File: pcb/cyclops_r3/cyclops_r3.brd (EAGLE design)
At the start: 69.8 x 53.3 mm, 78 parts, among them Q1 SUM11006, Q2 IRF510, U1 MCP4921, U2 TLV37, U3 317-N, U4 337-N, U5 ADR03, U6 OP1177, U7 LM324N, U8 ZXTD45

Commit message: While breadboarding the overcurrent protection circuit, I found a problem with the PFET power switch. Documented in notes, but not fixed yet.
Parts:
- C5: value 10pF -> 10nF
- R11: value 3.0k -> 3k
- R12: value 2.4k -> 3k
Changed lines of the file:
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@@
 <attribute name="NAME" x="14.813" y="20.8089" size="0.889" layer="26" font="vector" ratio="18" rot="MR180"/>
 </element>
-<element name="R12" library="cyclops" package="0603" value="2.4k" x="57.531" y="22.479" smashed="yes" rot="MR0">
+<element name="R12" library="cyclops" package="0603" value="3k" x="57.531" y="22.479" smashed="yes" rot="MR0">
 <attribute name="MN" value="Panasonic" x="56.007" y="39.243" size="1.6764" layer="28" ratio="18" rot="MR0" display="off"/>
 <attribute name="DK" value="PxxxxHTR-ND" x="56.007" y="39.243" size="1.6764" layer="28" ratio="18" rot="MR0" display="off"/>
@@
 <attribute name="VALUE" x="31.115" y="4.445" size="0.889" layer="28" font="vector" ratio="18" rot="MR0" align="center-left"/>
 </element>
-<element name="R11" library="cyclops" package="0603" value="3.0k" x="57.531" y="20.701" smashed="yes" rot="MR0">
+<element name="R11" library="cyclops" package="0603" value="3k" x="57.531" y="20.701" smashed="yes" rot="MR0">
 <attribute name="MN" value="Panasonic" x="56.134" y="27.305" size="1.6764" layer="28" ratio="18" rot="MR0" display="off"/>
 <attribute name="DK" value="PxxxxHTR-ND" x="56.134" y="27.305" size="1.6764" layer="28" ratio="18" rot="MR0" display="off"/>
@@
 <attribute name="VALUE" x="61.976" y="18.415" size="1.27" layer="27"/>
 </element>
-<element name="C5" library="cyclops" package="0603" value="10pF" x="39.116" y="6.604" smashed="yes" rot="MR180">
+<element name="C5" library="cyclops" package="0603" value="10nF" x="39.116" y="6.604" smashed="yes" rot="MR180">
 <attribute name="NAME" x="46.609" y="6.604" size="0.889" layer="26" font="vector" ratio="18" rot="MR180" align="center-right"/>
 <attribute name="VALUE" x="41.275" y="6.604" size="0.889" layer="28" font="vector" ratio="18" rot="MR180" align="center-left"/>
@@
 <wire x1="13.462" y1="27.94" x2="13.462" y2="26.416" width="0.4064" layer="16"/>
 <contactref element="VBIAS" pad="TP"/>
-<wire x1="17.018" y1="37.338" x2="17.018" y2="37.846" width="0" layer="19" extent="1-16"/>
 <wire x1="17.018" y1="37.846" x2="17.018" y2="39.116" width="0.4064" layer="16"/>
 <wire x1="18.362" y1="41.148" x2="22.292" y2="41.148" width="0.4064" layer="1"/>

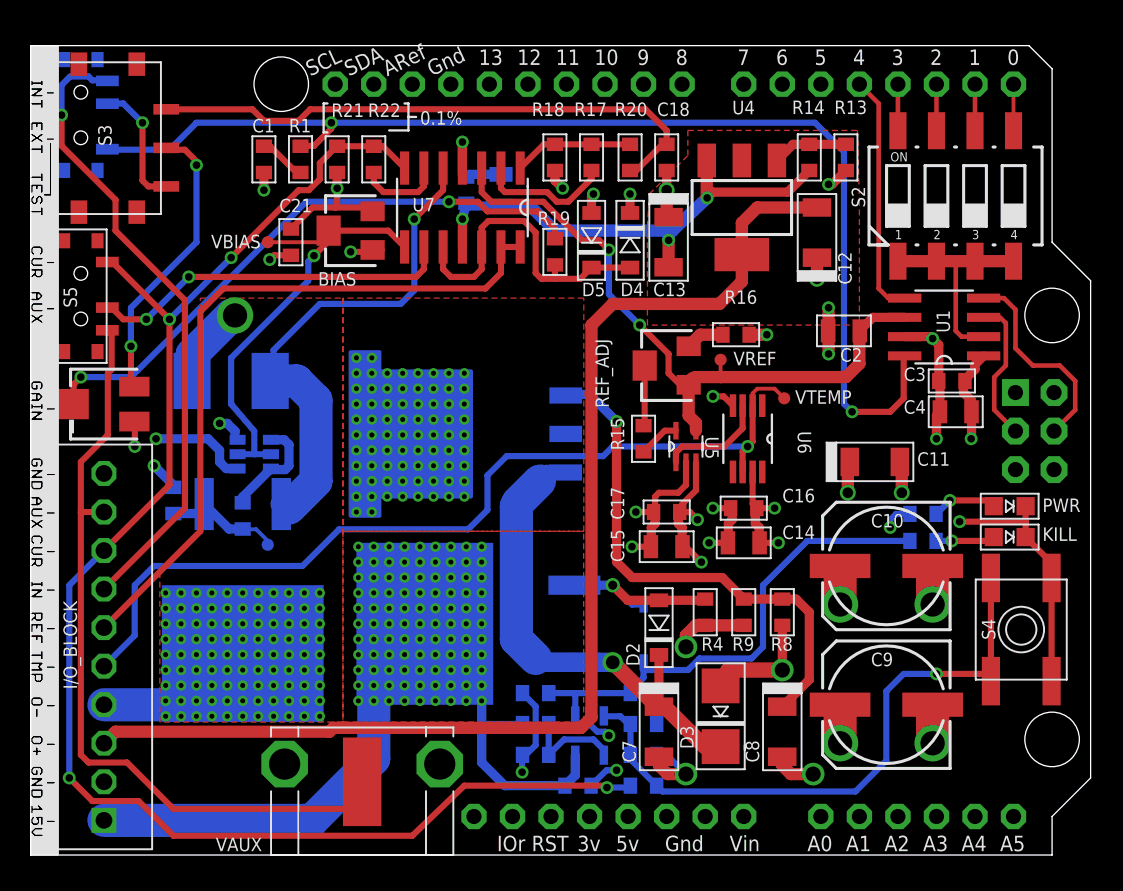
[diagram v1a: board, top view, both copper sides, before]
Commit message: Fixing the overcurrent protection circuit.
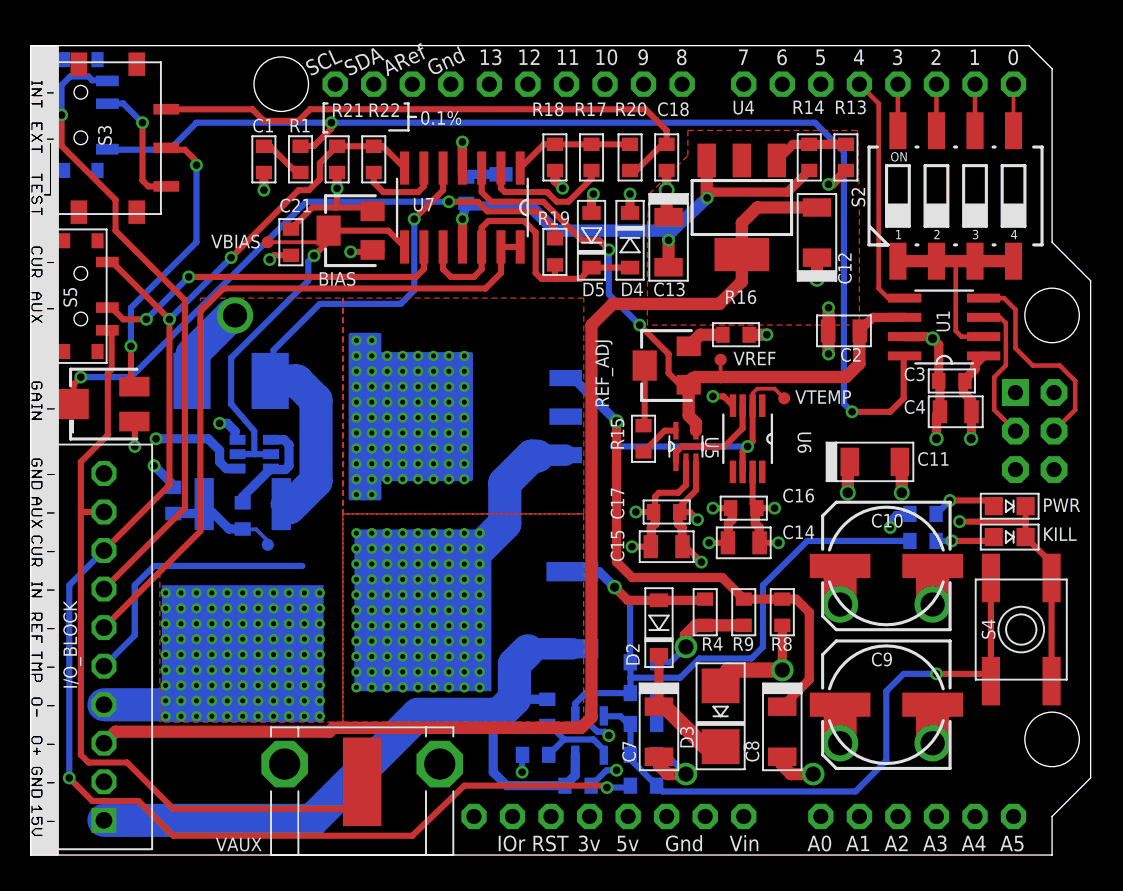
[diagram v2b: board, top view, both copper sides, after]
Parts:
- removed D1: (no value), cyclops:SOD-323F
- moved R10 7.40 mm to (39.1, 12.7), turned to 0 degrees
- moved U3 1.14 mm to (26.8, 28.9)
- moved R3 1.08 mm to (32.8, 9.40), turned to 270 degrees
- moved Q1 0.90 mm to (29.1, 16.1)
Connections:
- removed net +15V_RECT: C7.+, D2.C, D3.C, Q1.S, U3.3
- removed net N$18: D1.C, D2.A, Q1.G, R4.2
- new net +15V_ON: C7.+, D2.C, D3.C, Q1.D, U3.3
- net +15V: now also Q1.S; no longer Q1.D
- net KILL: now also D2.A, Q1.G, R4.2; no longer D1.A
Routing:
- net +15V_RECT: track 33.0 -> 0.00 mm, vias 1 -> 0
- net VTEMP: track 59.6 -> 34.6 mm
- net +15V_ON: track 0.00 -> 24.9 mm, vias 0 -> 99
- net KILL: track 32.7 -> 46.5 mm, vias 0 -> 1
- net N$18: track 11.6 -> 0.00 mm, vias 1 -> 0
- net +15V: track 47.2 -> 50.3 mm, vias 99 -> 0
- net GND: track 106.8 -> 104.3 mm
- net N$5: track 6.72 -> 6.19 mm
- added copper zone on layer 1, net +15V_ON
- removed copper zone on layer 1, net +15V

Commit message: Almost finished with the layout. I need to fix the top silskcreen which provides pin information.
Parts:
- removed D5: DS11015, cyclops:SOD123
- added C22: .1uF, cyclops:0603
- added D1: MMSZ, cyclops:SOD123
- C21: value .1uF -> ??
- D2: value MMSZ -> S1B; device cyclops:SOD123 -> cyclops:SMA-DO214AC
- D3: value S1B -> DS11015; device cyclops:SMA-DO214AC -> cyclops:SOD123
- KILL, PWR: value (none) -> LED
- R3: value 56k -> 10k
- R4: value 10k -> 56k
- U2: value TLV37 -> 317-N; device ti-extended:SOT95P280X145-5N -> cyclops:TO-263
- U3: value 317-N -> TLV37; device cyclops:TO-263 -> ti-extended:SOT95P280X145-5N
- U7: value LM324N -> TLV2374
- VAUX: value (none) -> 361V509E
- moved D3 31.9 mm to (38.2, 40.5), turned to 90 degrees
- moved U2 22.8 mm to (26.8, 28.9)
- moved U3 22.8 mm to (35.6, 7.87)
- moved C7 18.8 mm to (39.0, 26.9), turned to 90 degrees
- moved R3 12.3 mm to (43.2, 16.0), flipped to the top, turned to 90 degrees
- moved R4 12.3 mm to (32.8, 9.40), flipped to the bottom, turned to 270 degrees
- moved C21 8.09 mm to (21.8, 45.8), turned to 270 degrees
- moved D2 7.12 mm to (44.2, 9.14)
- moved R15 6.14 mm to (37.2, 33.3)
- moved D4 2.54 mm to (35.7, 40.5), turned to 270 degrees
- moved R1 1.91 mm to (14.6, 45.8)
- moved C1 1.90 mm to (12.2, 45.8)
- moved R21 1.90 mm to (17.0, 45.8)
- moved R22 1.90 mm to (19.4, 45.8)
- moved C11 0.25 mm to (54.1, 25.9)
- renumbered U$1 to ARDUNIO
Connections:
- net +12V: now also C22.1, D2.A, D3.C, U2.2, U2.4; no longer C21.1, D3.A, D4.C, U3.2, U3.4
- net +15V: now also R4.1, U3.5; no longer R3.1, U2.5
- net +15V_ON: now also D1.C, U2.3; no longer D3.C, U3.3
- net COMP+: now also U3.3; no longer U2.3
- net GND: now also C22.2, D4.A, R3.1, U3.2; no longer C21.2, D5.A, R4.1, U2.2
- net KILL: now also D1.A, R3.2, U3.1; no longer D2.A, R4.2, U2.1
- net N$15: now also C21.2
- net N$5: now also R4.2, U3.4; no longer R3.2, U2.4
- net N$72: now also U2.1; no longer U3.1
- net VI: now also C21.1
- net _VREF: now also D3.A, D4.C; no longer D4.A, D5.C
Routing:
- net VTEMP: track 34.6 -> 60.0 mm
- net +15V_ON: track 24.9 -> 49.1 mm, vias 99 -> 101
- net DACA: track 77.0 -> 69.6 mm
- net N$20: track 2.71 -> 7.42 mm, vias 0 -> 2
- net N$15: track 5.59 -> 8.84 mm
- net VI: track 100.2 -> 101.6 mm
- net GND: track 104.3 -> 102.9 mm, vias 31 -> 32
- net N$22: track 4.25 -> 3.64 mm

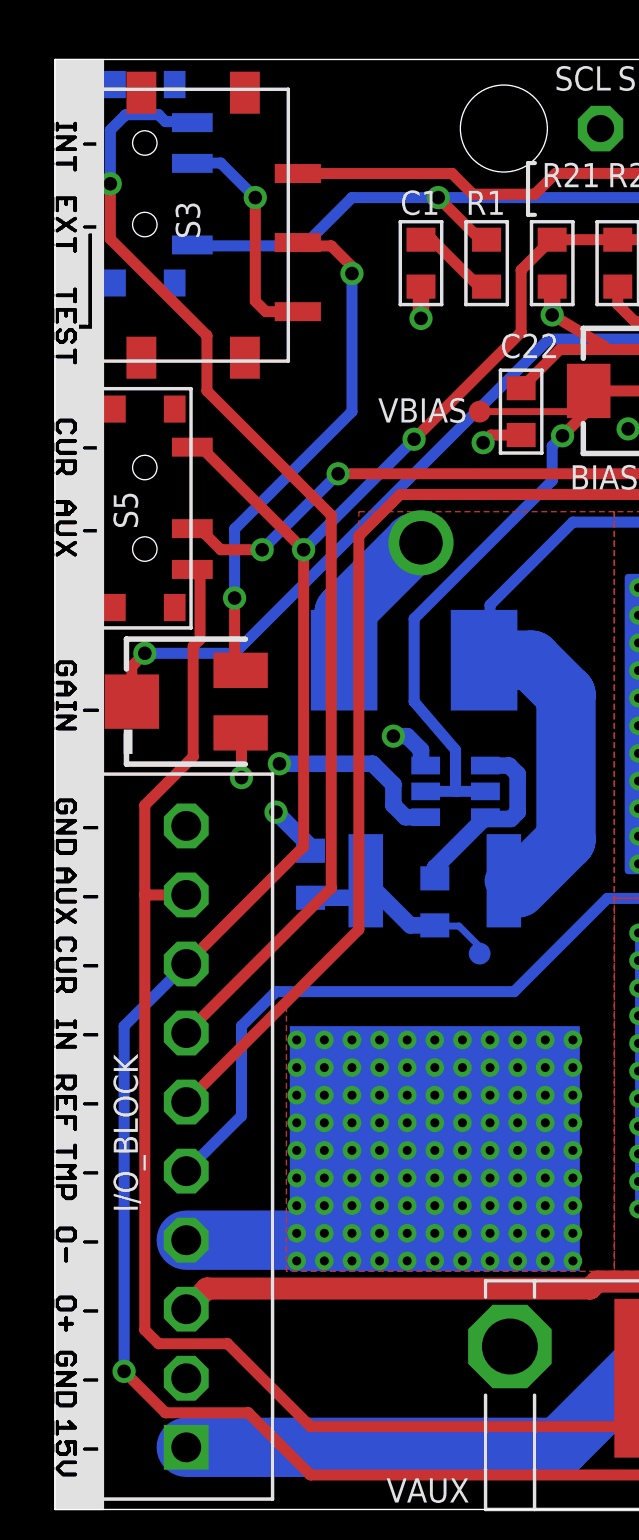
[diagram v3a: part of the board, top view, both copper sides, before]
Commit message: Almost done fixing the top/bottom side I/O labels. Also, found a big mistake in the 10-pin screw terminal header: I replaced the +LED supply with the -5V supply rail. I had to shift all the pins to get that LED pin back and I have not finished rerouting the board.
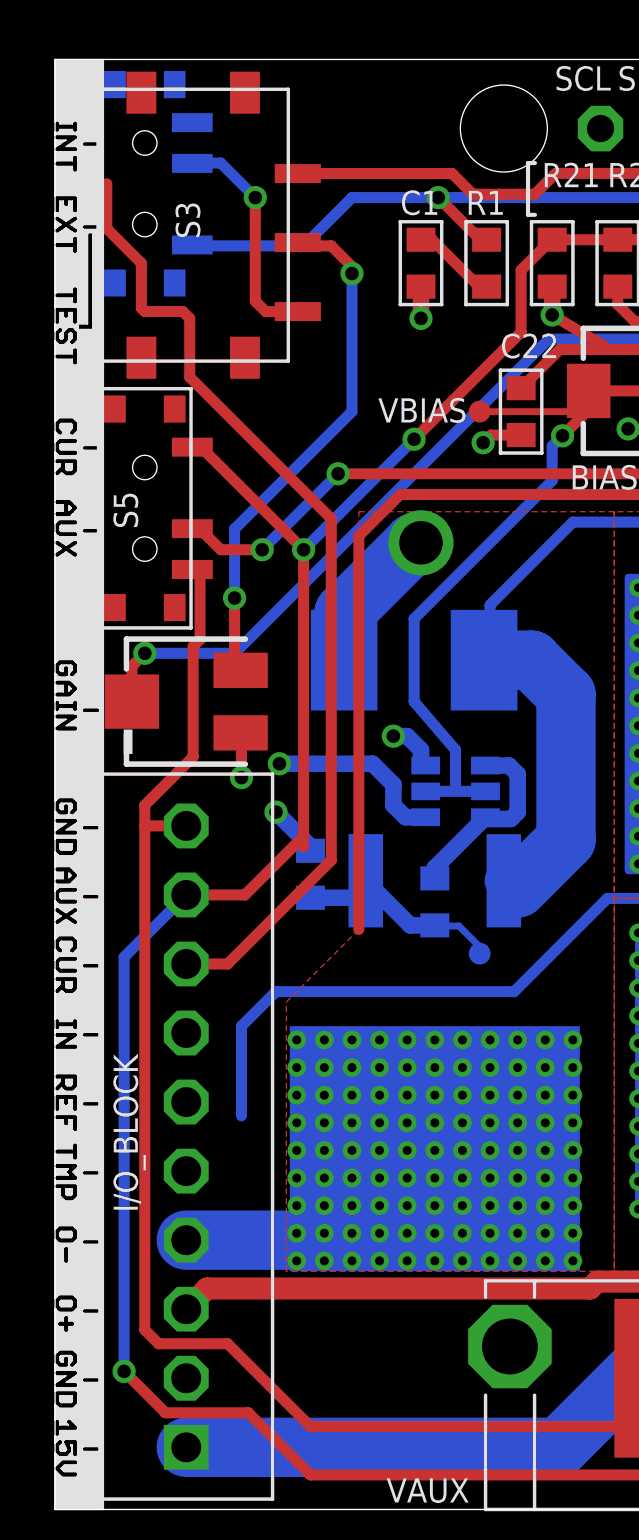
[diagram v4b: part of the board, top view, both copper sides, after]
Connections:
- net +12V: now also I/O_BLOCK.P$4
- net GND: no longer I/O_BLOCK.P$10
- net LED-: now also I/O_BLOCK.P$5; no longer I/O_BLOCK.P$4
- net VAUX: now also I/O_BLOCK.P$10; no longer I/O_BLOCK.P$9
- net VI: now also I/O_BLOCK.P$9; no longer I/O_BLOCK.P$8
- net VINPUT: now also I/O_BLOCK.P$8; no longer I/O_BLOCK.P$7
- net VREF: now also I/O_BLOCK.P$7; no longer I/O_BLOCK.P$6
- net VTEMP: now also I/O_BLOCK.P$6; no longer I/O_BLOCK.P$5
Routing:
- net LED-: track 18.7 -> 4.22 mm, vias 99 -> 98
- net +12V: track 52.9 -> 67.4 mm, vias 90 -> 91
- net VREF: track 47.3 -> 38.3 mm
- net VINPUT: track 42.2 -> 36.0 mm, vias 1 -> 0
- net VTEMP: track 60.0 -> 57.1 mm
- net VI: track 101.6 -> 103.2 mm

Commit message: Should be finished. Do one last check before placing order.
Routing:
- net LED-: track 4.22 -> 12.5 mm, vias 98 -> 99
- net VREF: track 38.3 -> 46.2 mm
- net VINPUT: track 36.0 -> 41.1 mm, vias 0 -> 1
- net VTEMP: track 57.1 -> 57.7 mm
- net +12V: vias 91 -> 90

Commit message: Board sent to fab house. Doing some directory clean up now.
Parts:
- Q2: value IRF510 -> IRF540
- S4: value UNKILL -> REVIVE
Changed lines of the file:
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@@
 <layers>
 <layer number="1" name="Top" color="4" fill="1" visible="yes" active="yes"/>
-<layer number="2" name="Route2" color="1" fill="3" visible="no" active="yes"/>
+<layer number="2" name="Route2" color="1" fill="3" visible="yes" active="yes"/>
 <layer number="3" name="Route3" color="4" fill="3" visible="no" active="no"/>
 <layer number="4" name="Route4" color="1" fill="4" visible="no" active="no"/>
@@
 <layer number="13" name="Route13" color="4" fill="5" visible="no" active="no"/>
 <layer number="14" name="Route14" color="1" fill="6" visible="no" active="no"/>
-<layer number="15" name="Route15" color="4" fill="6" visible="no" active="yes"/>
+<layer number="15" name="Route15" color="4" fill="6" visible="yes" active="yes"/>
 <layer number="16" name="Bottom" color="1" fill="1" visible="yes" active="yes"/>
 <layer number="17" name="Pads" color="2" fill="1" visible="yes" active="yes"/>
@@
 <layer number="21" name="tPlace" color="7" fill="1" visible="yes" active="yes"/>
 <layer number="22" name="bPlace" color="7" fill="1" visible="yes" active="yes"/>
-<layer number="23" name="tOrigins" color="15" fill="1" visible="no" active="yes"/>
-<layer number="24" name="bOrigins" color="15" fill="1" visible="no" active="yes"/>
+<layer number="23" name="tOrigins" color="15" fill="1" visible="yes" active="yes"/>
+<layer number="24" name="bOrigins" color="15" fill="1" visible="yes" active="yes"/>
 <layer number="25" name="tNames" color="7" fill="1" visible="yes" active="yes"/>
 <layer number="26" name="bNames" color="7" fill="1" visible="yes" active="yes"/>
 <layer number="27" name="tValues" color="7" fill="1" visible="yes" active="yes"/>
 <layer number="28" name="bValues" color="7" fill="1" visible="yes" active="yes"/>
-<layer number="29" name="tStop" color="7" fill="3" visible="yes" active="yes"/>
-<layer number="30" name="bStop" color="7" fill="6" visible="yes" active="yes"/>
+<layer number="29" name="tStop" color="7" fill="3" visible="no" active="yes"/>
+<layer number="30" name="bStop" color="7" fill="6" visible="no" active="yes"/>
 <layer number="31" name="tCream" color="7" fill="4" visible="no" active="yes"/>
 <layer number="32" name="bCream" color="7" fill="5" visible="no" active="yes"/>
@@
 <attribute name="NAME" x="17.399" y="25.781" size="0.889" layer="26" font="vector" ratio="18" rot="MR90"/>
 </element>
-<element name="Q2" library="cyclops" package="TO-262_01" value="IRF510" x="12.7" y="17.78" smashed="yes" rot="MR180">
+<element name="Q2" library="cyclops" package="TO-262_01" value="IRF540" x="12.7" y="17.78" smashed="yes" rot="MR180">
 <attribute name="NAME" x="5.842" y="9.144" size="0.889" layer="26" font="vector" ratio="18" rot="MR90"/>
 <attribute name="VALUE" x="5.842" y="11.938" size="0.889" layer="28" font="vector" ratio="18" rot="MR90"/>
@@
 </element>
 <element name="BIAS" library="cyclops" package="SM-42/43W" value="10k" x="19.812" y="41.148" smashed="yes" rot="R90">
-<attribute name="NAME" x="17.666" y="37.523" size="0.889" layer="25" font="vector" ratio="18"/>
-<attribute name="VALUE" x="20.968" y="37.527" size="0.889" layer="27" font="vector" ratio="18"/>
+<attribute name="NAME" x="18.047" y="37.523" size="0.889" layer="25" font="vector" ratio="18"/>
+<attribute name="VALUE" x="21.349" y="37.527" size="0.889" layer="27" font="vector" ratio="18"/>
 </element>
 <element name="C22" library="cyclops" package="0603" value=".1uF" x="15.875" y="40.386" smashed="yes" rot="R90">
@@
 <attribute name="MPN" value="Dialight" x="77.978" y="29.591" size="1.6764" layer="27" ratio="18" rot="R270" display="off"/>
 <attribute name="NAME" x="65.405" y="22.606" size="0.889" layer="25" font="vector" ratio="18"/>
-<attribute name="VALUE" x="61.214" y="19.558" size="0.889" layer="27" font="vector" ratio="18" rot="R90"/>
+<attribute name="VALUE" x="61.214" y="20.828" size="0.889" layer="27" font="vector" ratio="18" rot="R90"/>
 </element>
 <element name="R10" library="cyclops" package="0603" value="220k" x="39.116" y="12.7" smashed="yes" rot="MR0">
@@
 <attribute name="MPN" value="Dialight" x="67.818" y="27.051" size="1.6764" layer="27" ratio="18" rot="R270" display="off"/>
 <attribute name="NAME" x="65.405" y="20.701" size="0.889" layer="25" font="vector" ratio="18"/>
-<attribute name="VALUE" x="61.214" y="22.225" size="0.889" layer="27" font="vector" ratio="18" rot="R90"/>
 </element>
 <element name="C5" library="cyclops" package="0603" value="10nF" x="39.116" y="6.604" smashed="yes" rot="MR180">
@@
 <attribute name="VALUE" x="41.148" y="6.604" size="0.889" layer="28" font="vector" ratio="18" rot="MR180" align="center-left"/>
 </element>
-<element name="S4" library="cyclops" package="EVQ-Q2" value="UNKILL" x="64.008" y="14.859" smashed="yes" rot="R270">
+<element name="S4" library="cyclops" package="EVQ-Q2" value="REVIVE" x="64.008" y="14.859" smashed="yes" rot="R270">
 <attribute name="NAME" x="61.412" y="15.573" size="0.889" layer="25" font="vector" ratio="18" rot="R270"/>
 <attribute name="VALUE" x="67.336" y="17.043" size="0.889" layer="27" font="vector" ratio="18" rot="R270"/>
@@
 <wire x1="37.084" y1="15.367" x2="26.035" y2="15.367" width="0.6096" layer="16"/>
 <wire x1="26.035" y1="15.367" x2="25.273" y2="16.129" width="0.6096" layer="16"/>
-<wire x1="25.273" y1="16.129" x2="24.9555" y2="16.129" width="0" layer="19" extent="16-16"/>
+<wire x1="25.273" y1="16.129" x2="24.9555" y2="16.129" width="0.4064" layer="16"/>
 </signal>
 <signal name="+12V" class="1">
@@
 <wire x1="3.556" y1="9.906" x2="12.7" y2="9.906" width="2.1844" layer="16"/>
 <wire x1="12.7" y1="9.906" x2="12.7" y2="15.24" width="2.1844" layer="16"/>
-<wire x1="46.7614" y1="20.574" x2="46.736" y2="20.574" width="0" layer="19" extent="1-1"/>
-<wire x1="24.257" y1="28.8925" x2="24.257" y2="28.829" width="0" layer="19" extent="16-16"/>
-<wire x1="33.9852" y1="28.8925" x2="27.305" y2="28.829" width="0" layer="19" extent="16-16"/>
+<wire x1="46.7614" y1="20.574" x2="46.736" y2="20.574" width="0.4064" layer="1"/>
+<wire x1="24.257" y1="28.8925" x2="24.257" y2="28.829" width="0.4064" layer="16"/>
+<wire x1="27.305" y1="28.829" x2="33.9852" y2="28.8925" width="0" layer="19" extent="16-16"/>
 </signal>
 <signal name="N$72">
@@
 <wire x1="3.556" y1="12.446" x2="11.43" y2="12.446" width="2.1844" layer="1"/>
 <wire x1="11.43" y1="12.446" x2="11.684" y2="12.192" width="2.1844" layer="1"/>
-<wire x1="12.7" y1="13.208" x2="12.7" y2="13.6525" width="0" layer="19" extent="16-16"/>
+<wire x1="12.7" y1="13.6525" x2="12.7" y2="13.208" width="0.4064" layer="16"/>
 </signal>
 <signal name="REFA">
